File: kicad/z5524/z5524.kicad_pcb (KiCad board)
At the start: 4 copper layers, 80 x 80 mm, 21 parts, among them J1 Conn_01x01, J2 Conn_01x02, J3 Conn_02x20_Odd_Even, U13 LM4040AIM3-2.5, U14 AD5328, U15 M24C02-WMN, U7 PCA9555D

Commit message: schematic drafted- still needs some updates
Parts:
- removed G***: LOGO, project_footprints:zoxnoxious_small
- removed H1, H2, H3, H4: MountingHole, MountingHole:MountingHole_3.2mm_M3
- added C1: 0.1u, Capacitor_SMD:C_0603_1608Metric, F.Cu at (225.9, 34.9)
- added C10: 1u, Capacitor_SMD:C_1206_3216Metric, F.Cu at (170.7, 57.1)
- added C11: 1u, Capacitor_SMD:C_1206_3216Metric, F.Cu at (168.8, 62.8)
- added C12: 10n, Capacitor_SMD:C_0603_1608Metric, F.Cu at (214.0, 61.0)
- added C14: 1u, Capacitor_SMD:C_0603_1608Metric, F.Cu at (222.7, 53.4)
- added C15: 1u, Capacitor_SMD:C_0603_1608Metric, F.Cu at (218.0, 61.0)
- added C16: 1u, Capacitor_SMD:C_0603_1608Metric, F.Cu at (214.4, 58.5)
- added C17: 0.1u, Capacitor_SMD:C_0603_1608Metric, F.Cu at (218.4, 55.9)
- added C18: 0.1u, Capacitor_SMD:C_0603_1608Metric, F.Cu at (202.0, 63.0)
- added C19: 22n, Capacitor_SMD:C_0603_1608Metric, F.Cu at (221.9, 32.4)
- added C2: 0.1u, Capacitor_SMD:C_0603_1608Metric, F.Cu at (213.9, 30.3)
- added C20: 2u2, Capacitor_SMD:C_0603_1608Metric, F.Cu at (221.9, 34.9)
- added C21: 2u2, Capacitor_SMD:C_0603_1608Metric, F.Cu at (196.2, 89.1)
- added C22: 15n, Capacitor_SMD:C_0603_1608Metric, F.Cu at (217.5, 40.4)
- added C23: 1n, Capacitor_SMD:C_0603_1608Metric, F.Cu at (234.2, 24.9)
- added C26: 47n, Capacitor_SMD:C_0805_2012Metric, F.Cu at (205.7, 35.3)
- added C27: 22n, Capacitor_SMD:C_0603_1608Metric, F.Cu at (217.9, 30.3)
- added C28: 22n, Capacitor_SMD:C_0603_1608Metric, F.Cu at (209.9, 35.1)
- added C29: 22n, Capacitor_SMD:C_0603_1608Metric, F.Cu at (213.9, 27.8)
- added C3: 1u, Capacitor_SMD:C_1206_3216Metric_Pad1.33x1.80mm_HandSolder, F.Cu at (162.4, 68.6)
- added C30: 0.1u, Capacitor_SMD:C_0603_1608Metric, F.Cu at (254.7, 50.0)
- added C31: 0.1u, Capacitor_SMD:C_0603_1608Metric, F.Cu at (247.6, 52.5)
- added C32: 560pF, Capacitor_SMD:C_0603_1608Metric, F.Cu at (242.0, 60.0)
- added C33: 33nF, Capacitor_SMD:C_0603_1608Metric, F.Cu at (243.6, 53.3)
- added C34: 33nF, Capacitor_SMD:C_0603_1608Metric, F.Cu at (251.6, 52.5)
- added C35: 33nF, Capacitor_SMD:C_0603_1608Metric, F.Cu at (246.0, 58.4)
- added C36: 4.7u, Capacitor_THT:C_Rect_L7.2mm_W5.5mm_P5.00mm_FKS2_FKP2_MKS2_MKP2, F.Cu at (233.6, 49.7)
- added C38: 2n, Capacitor_SMD:C_1206_3216Metric, F.Cu at (234.5, 54.9)
- added C4: 1u, Capacitor_SMD:C_1206_3216Metric_Pad1.33x1.80mm_HandSolder, F.Cu at (177.4, 51.3)
- added C40: 0.1u, Capacitor_SMD:C_0603_1608Metric, F.Cu at (243.3, 32.4)
- added C41: 0.1u, Capacitor_SMD:C_0603_1608Metric, F.Cu at (251.3, 32.4)
- added C42: 0.1u, Capacitor_SMD:C_0603_1608Metric, F.Cu at (255.3, 29.9)
- added C43: 33p, Capacitor_SMD:C_0603_1608Metric, F.Cu at (243.3, 27.4)
- added C44: 33p, Capacitor_SMD:C_0603_1608Metric, F.Cu at (247.3, 29.9)
- added C45: 0.1u, Capacitor_SMD:C_0603_1608Metric, F.Cu at (204.6, 78.8)
- added C46: 0.1u, Capacitor_SMD:C_0603_1608Metric, F.Cu at (208.6, 76.8)
- added C47: 0.1u, Capacitor_SMD:C_0603_1608Metric, F.Cu at (204.6, 81.3)
- added C48: 10u, Capacitor_SMD:C_0805_2012Metric, F.Cu at (186.8, 25.1)
- added C49: 3.9n, Capacitor_SMD:C_0603_1608Metric, F.Cu at (185.1, 37.9)
- added C5: 0.1u, Capacitor_SMD:C_0603_1608Metric, F.Cu at (190.0, 58.5)
- added C50: 0.1u, Capacitor_SMD:C_0603_1608Metric, F.Cu at (204.9, 74.2)
- added C51: 100p, Capacitor_SMD:C_0805_2012Metric, F.Cu at (172.8, 37.8)
- added C52: 100p, Capacitor_SMD:C_0805_2012Metric, F.Cu at (166.5, 43.0)
- added C53: 100p, Capacitor_SMD:C_0805_2012Metric, F.Cu at (179.1, 31.6)
- added C54: 0.1u, Capacitor_SMD:C_0603_1608Metric, F.Cu at (208.6, 79.3)
- added C55: 0.1u, Capacitor_SMD:C_0603_1608Metric, F.Cu at (212.9, 74.2)
- added C56: 4u7, Capacitor_THT:CP_Radial_D4.0mm_P1.50mm, F.Cu at (181.1, 26.4)
- added C57: 4.7u, Capacitor_SMD:C_0805_2012Metric, F.Cu at (202.2, 57.8)
- added C58: 0.1u, Capacitor_SMD:C_0603_1608Metric, F.Cu at (210.7, 50.9)
- added C59: 100p, Capacitor_SMD:C_0603_1608Metric, F.Cu at (181.6, 62.3)
- added C6: 0.1u, Capacitor_SMD:C_0603_1608Metric, F.Cu at (186.0, 58.5)
- added C60: 0.1u, Capacitor_SMD:C_0603_1608Metric, F.Cu at (181.1, 68.3)
- added C61: 0.1u, Capacitor_SMD:C_0603_1608Metric, F.Cu at (185.6, 61.0)
- added C62: 100p, Capacitor_SMD:C_0603_1608Metric, F.Cu at (187.3, 50.9)
- added C63: 22n, Capacitor_SMD:C_0603_1608Metric, F.Cu at (206.4, 57.5)
- added C64: 0.1u, Capacitor_SMD:C_0603_1608Metric, F.Cu at (246.7, 47.4)
- added C65: 0.1u, Capacitor_SMD:C_0603_1608Metric, F.Cu at (254.7, 47.4)
- added C66: 5n, Capacitor_SMD:C_0603_1608Metric, F.Cu at (251.3, 24.9)
- added C67: 33p, Capacitor_SMD:C_0603_1608Metric, F.Cu at (255.3, 27.4)
- added C68: 0.1u, Capacitor_SMD:C_0603_1608Metric, F.Cu at (208.9, 74.2)
- added C69: 0.1u, Capacitor_SMD:C_0603_1608Metric, F.Cu at (212.6, 76.8)
- added C7: 0.1u, Capacitor_SMD:C_0603_1608Metric, F.Cu at (191.3, 50.9)
- added C70: 10n, Capacitor_SMD:C_0603_1608Metric, F.Cu at (177.0, 37.5)
- added C71: 10n, Capacitor_SMD:C_0603_1608Metric, F.Cu at (183.3, 32.9)
- added C72: 6.8n, Capacitor_SMD:C_0603_1608Metric, F.Cu at (222.4, 55.9)
- added C73: 6.8n, Capacitor_SMD:C_0603_1608Metric, F.Cu at (210.0, 62.5)
- added C74: 22n, Capacitor_SMD:C_0603_1608Metric, F.Cu at (221.5, 40.4)
- added C8: 0.1u, Capacitor_SMD:C_0603_1608Metric, F.Cu at (186.0, 55.9)
- added C9: 22n, Capacitor_SMD:C_0603_1608Metric, F.Cu at (206.0, 60.5)
- added D1: 1N5819WS, Diode_SMD:D_SOD-323, F.Cu at (214.0, 25.1)
- added D2: 1N4148WS, Diode_SMD:D_SOD-323, F.Cu at (239.5, 54.7)
- added D3: 1N4148WS, Diode_SMD:D_SOD-323, F.Cu at (233.8, 58.1)
- added D5: 1N4148WS, Diode_SMD:D_SOD-323, F.Cu at (242.6, 47.7)
- added D6: 1N4148WS, Diode_SMD:D_SOD-323, F.Cu at (242.6, 50.6)
- added Q1: 2N7002K, Package_TO_SOT_SMD:SOT-23, F.Cu at (161.9, 43.7)
- added R1: 1k, Resistor_SMD:R_1206_3216Metric, F.Cu at (176.3, 57.1)
- added R10: 5k1, Resistor_SMD:R_0603_1608Metric, F.Cu at (218.7, 53.4)
- added R11: 20k, Resistor_SMD:R_0603_1608Metric, F.Cu at (190.0, 55.9)
- added R12: 10k, Resistor_SMD:R_0603_1608Metric, F.Cu at (218.7, 50.9)
- added R13: 10k, Resistor_SMD:R_0603_1608Metric, F.Cu at (191.3, 53.4)
- added R14: 22k, Resistor_SMD:R_0603_1608Metric, F.Cu at (214.4, 55.9)
- added R15: 22k, Resistor_SMD:R_0603_1608Metric, F.Cu at (218.4, 58.5)
- added R16: 20k, Resistor_SMD:R_0603_1608Metric, F.Cu at (173.1, 68.3)
- added R17: 10k, Resistor_SMD:R_0603_1608Metric, F.Cu at (206.0, 63.0)
- added R18: 110, Resistor_SMD:R_0603_1608Metric, F.Cu at (218.0, 63.5)
- added R19: 110, Resistor_SMD:R_0603_1608Metric, F.Cu at (214.7, 50.9)
- added R2: 240, Resistor_SMD:R_1206_3216Metric, F.Cu at (168.2, 68.5)
- added R21: 110, Resistor_SMD:R_0603_1608Metric, F.Cu at (210.4, 57.5)
- added R22: 5k1, Resistor_SMD:R_0603_1608Metric, F.Cu at (217.9, 35.3)
- added R23: 110k, Resistor_SMD:R_0603_1608Metric, F.Cu at (213.9, 35.3)
- added R24: 10k, Resistor_SMD:R_0603_1608Metric, F.Cu at (221.9, 27.4)
- added R25: 20k, Resistor_SMD:R_0603_1608Metric, F.Cu at (229.9, 29.9)
- added R26: 47k, Resistor_SMD:R_0603_1608Metric, F.Cu at (225.5, 37.4)
- added R27: 20k, Resistor_SMD:R_0603_1608Metric, F.Cu at (225.9, 29.9)
- added R28: 36k, Resistor_SMD:R_0603_1608Metric, F.Cu at (209.5, 38.1)
- added R29: 30k, Resistor_SMD:R_0603_1608Metric, F.Cu at (213.5, 40.4)
- added R3: ?, Resistor_SMD:R_1206_3216Metric, F.Cu at (176.3, 60.4)
- added R30: 39k, Resistor_SMD:R_0603_1608Metric, F.Cu at (209.5, 40.6)
- added R31: 10k, Resistor_SMD:R_0603_1608Metric, F.Cu at (217.5, 37.8)
- added R32: 15k, Resistor_SMD:R_0603_1608Metric, F.Cu at (225.9, 32.4)
- added R33: 51k, Resistor_SMD:R_0603_1608Metric, F.Cu at (205.4, 38.1)
- added R34: 47k, Resistor_SMD:R_0603_1608Metric, F.Cu at (213.9, 32.8)
- added R35: 11k, Resistor_SMD:R_0603_1608Metric, F.Cu at (221.5, 37.8)
- added R36: 5k1, Resistor_SMD:R_0603_1608Metric, F.Cu at (217.9, 32.8)
- added R37: 22k, Resistor_SMD:R_0603_1608Metric, F.Cu at (225.9, 27.4)
- added R38: 4k7, Resistor_SMD:R_0603_1608Metric, F.Cu at (218.2, 24.9)
- added R39: 4k7, Resistor_SMD:R_0603_1608Metric, F.Cu at (226.2, 24.9)
- added R4: R, Resistor_SMD:R_0603_1608Metric, F.Cu at (177.6, 63.3)
- added R40: 5k1, Resistor_SMD:R_0603_1608Metric, F.Cu at (233.9, 27.4)
- added R41: 5k1, Resistor_SMD:R_0603_1608Metric, F.Cu at (229.9, 27.4)
- added R42: 100k, Resistor_SMD:R_0603_1608Metric, F.Cu at (205.4, 40.6)
- added R43: 5k1, Resistor_SMD:R_0603_1608Metric, F.Cu at (221.9, 29.9)
- added R44: 1M, Resistor_SMD:R_0603_1608Metric, F.Cu at (213.5, 37.8)
- added R45: 47k, Resistor_SMD:R_0603_1608Metric, F.Cu at (217.9, 27.8)
- added R46: 68k, Resistor_SMD:R_0603_1608Metric, F.Cu at (250.7, 50.0)
- added R48: 240k, Resistor_SMD:R_0603_1608Metric, F.Cu at (246.0, 55.9)
- added R49: 500, Resistor_SMD:R_0603_1608Metric, F.Cu at (250.7, 47.4)
- added R5: ?, Resistor_SMD:R_0603_1608Metric, F.Cu at (173.6, 63.3)
- added R50: 1k, Resistor_SMD:R_0603_1608Metric, F.Cu at (237.9, 57.8)
- added R51: 20k, Resistor_SMD:R_0603_1608Metric, F.Cu at (187.3, 53.4)
- added R52: 62k, Resistor_SMD:R_0603_1608Metric, F.Cu at (246.7, 50.0)
- added R53: 47k, Resistor_SMD:R_0603_1608Metric, F.Cu at (247.3, 24.9)
- added R54: 47k, Resistor_SMD:R_0603_1608Metric, F.Cu at (251.3, 29.9)
- added R55: 47k, Resistor_SMD:R_0603_1608Metric, F.Cu at (243.3, 24.9)
- added R57: 47k, Resistor_SMD:R_0603_1608Metric, F.Cu at (255.3, 24.9)
- added R58: 4k3, Resistor_SMD:R_0603_1608Metric, F.Cu at (178.8, 34.3)
- added R59: 47k, Resistor_SMD:R_0603_1608Metric, F.Cu at (191.1, 27.4)
- added R6: 13k, Resistor_SMD:R_0603_1608Metric, F.Cu at (177.1, 68.3)
- added R60: 49.9k, Resistor_SMD:R_0603_1608Metric, F.Cu at (180.6, 40.1)
- added R61: 10k, Resistor_SMD:R_0603_1608Metric, F.Cu at (189.1, 37.9)
- added R62: 270k, Resistor_SMD:R_0603_1608Metric, F.Cu at (185.1, 35.4)
- added R63: 100k, Resistor_SMD:R_0603_1608Metric, F.Cu at (183.3, 30.4)
- added R64: 22k, Resistor_SMD:R_0603_1608Metric, F.Cu at (186.6, 27.9)
- added R65: 270, Resistor_SMD:R_0603_1608Metric, F.Cu at (191.3, 32.4)
- added R66: 20k, Resistor_SMD:R_0603_1608Metric, F.Cu at (195.1, 27.4)
- added R67: 20k, Resistor_SMD:R_0603_1608Metric, F.Cu at (170.8, 43.1)
- added R68: 20k, Resistor_SMD:R_0603_1608Metric, F.Cu at (191.3, 29.9)
- added R69: 20k, Resistor_SMD:R_0603_1608Metric, F.Cu at (195.3, 32.4)
- added R7: 3k, Resistor_SMD:R_0603_1608Metric, F.Cu at (181.1, 65.8)
- added R70: 20k, Resistor_SMD:R_0603_1608Metric, F.Cu at (178.8, 43.1)
- added R71: 20k, Resistor_SMD:R_0603_1608Metric, F.Cu at (187.3, 32.9)
- added R72: 100, Resistor_SMD:R_0603_1608Metric, F.Cu at (176.6, 40.6)
- added R73: 100k, Resistor_SMD:R_0603_1608Metric, F.Cu at (182.8, 42.6)
- added R74: 20k, Resistor_SMD:R_0603_1608Metric, F.Cu at (195.3, 29.9)
- added R75: 499k, Resistor_SMD:R_0603_1608Metric, F.Cu at (191.1, 24.9)
- added R76: 10k, Resistor_SMD:R_0603_1608Metric, F.Cu at (172.6, 40.6)
- added R77: 5k1, Resistor_SMD:R_0603_1608Metric, F.Cu at (214.7, 53.4)
- added R78: 22k, Resistor_SMD:R_0603_1608Metric, F.Cu at (210.0, 60.0)
- added R79: 1k, Resistor_SMD:R_0603_1608Metric, F.Cu at (242.0, 57.4)
- added R8: 6k8, Resistor_SMD:R_0603_1608Metric, F.Cu at (185.6, 63.5)
- added R80: 62k, Resistor_SMD:R_0603_1608Metric, F.Cu at (250.0, 55.0)
- added R81: 100, Resistor_SMD:R_0603_1608Metric, F.Cu at (247.3, 27.4)
- added R82: 4k7, Resistor_SMD:R_0603_1608Metric, F.Cu at (174.8, 43.1)
- added R83: 4k7, Resistor_SMD:R_0603_1608Metric, F.Cu at (189.1, 35.4)
- added R84: 4k7, Resistor_SMD:R_0603_1608Metric, F.Cu at (195.1, 24.9)
- added R85: 47k, Resistor_SMD:R_0603_1608Metric, F.Cu at (251.3, 27.4)
- added R86: 47k, Resistor_SMD:R_0603_1608Metric, F.Cu at (247.3, 32.4)
- added R87: 47k, Resistor_SMD:R_0603_1608Metric, F.Cu at (243.3, 29.9)
- added R88: 10k, Resistor_SMD:R_0603_1608Metric, F.Cu at (187.3, 30.4)
- added R89: 10k, Resistor_SMD:R_0603_1608Metric, F.Cu at (181.0, 36.8)
- added R9: 6k8, Resistor_SMD:R_0603_1608Metric, F.Cu at (173.1, 65.8)
- added R90: 1k, Resistor_SMD:R_0603_1608Metric, F.Cu at (181.1, 59.8)
- added R91: 1k, Resistor_SMD:R_0603_1608Metric, F.Cu at (177.1, 65.8)
- added R92: 18k, Resistor_SMD:R_0603_1608Metric, F.Cu at (222.7, 50.9)
- added R93: 18k, Resistor_SMD:R_0603_1608Metric, F.Cu at (214.0, 63.5)
- added R94: 82k, Resistor_SMD:R_0603_1608Metric, F.Cu at (210.7, 53.4)
- added R95: 82k, Resistor_SMD:R_0603_1608Metric, F.Cu at (202.0, 60.5)
- added R96: 10k, Resistor_SMD:R_0603_1608Metric, F.Cu at (230.2, 24.9)
- added R97: 10k, Resistor_SMD:R_0603_1608Metric, F.Cu at (222.2, 24.9)
- added RV1: 5k, Potentiometer_THT:Potentiometer_Bourns_3296W_Vertical, F.Cu at (176.0, 26.8)
- added RV2: 5k, Potentiometer_THT:Potentiometer_Bourns_3296W_Vertical, F.Cu at (172.8, 98.4)
- added RV3: 5k, Potentiometer_THT:Potentiometer_Bourns_3296W_Vertical, F.Cu at (167.6, 38.3)
- added U1: TL074, Package_SO:TSSOP-14_4.4x5mm_P0.65mm, F.Cu at (207.7, 28.7)
- added U10: TL072, Package_SO:SO-8_3.9x4.9mm_P1.27mm, F.Cu at (181.9, 76.2)
- added U11: NE5532, Package_SO:SOIC-8_3.9x4.9mm_P1.27mm, F.Cu at (180.1, 98.4)
- added U12: TL074, Package_SO:TSSOP-14_4.4x5mm_P0.65mm, F.Cu at (222.7, 85.8)
- added U16: SSI2130, Package_DFN_QFN:QFN-32-1EP_4x4mm_P0.4mm_EP2.65x2.65mm, F.Cu at (173.7, 33.2)
- added U17: DG442xY, Package_SO:SOIC-16_3.9x9.9mm_P1.27mm, F.Cu at (163.7, 29.3)
- added U18: TL072, Package_SO:SO-8_3.9x4.9mm_P1.27mm, F.Cu at (198.4, 80.8)
- added U19: LM311, Package_SO:TSSOP-8_4.4x3mm_P0.65mm, F.Cu at (198.5, 75.3)
- added U2: LM337L_TO92, Package_TO_SOT_THT:TO-92_Inline, F.Cu at (161.4, 64.4)
- added U21: AD5328, Package_SO:TSSOP-16_4.4x5mm_P0.65mm, F.Cu at (204.3, 53.0)
- added U3: LM4040BIM3-2.5, Package_TO_SOT_SMD:SOT-23, F.Cu at (181.6, 56.3)
- added U4: LM4040BIM3-4.1, Package_TO_SOT_SMD:SOT-23, F.Cu at (182.8, 51.9)
- added U5: DG442xY, Package_SO:SOIC-16_3.9x9.9mm_P1.27mm, F.Cu at (163.7, 55.4)
- added U6: TL072, Package_SO:SO-8_3.9x4.9mm_P1.27mm, F.Cu at (222.5, 76.2)
- added U8: LM78L05_TO92, Package_TO_SOT_THT:TO-92_Inline, F.Cu at (169.9, 52.9)
- added U9: AS3394, Package_SO:SOIC-24W_7.5x15.4mm_P1.27mm, F.Cu at (171.2, 81.5)
- R47: value 4k7 -> 1k; footprint Resistor_SMD:R_1206_3216Metric -> Resistor_SMD:R_0603_1608Metric
- U13: value LM4040AIM3-2.5 -> AS3364; footprint Package_TO_SOT_SMD:SOT-23 -> Package_SO:SOIC-16_3.9x9.9mm_P1.27mm
- moved J1 13.9 mm to (55.7, 72.1)
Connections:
- C39 pad 1: /DAC/VREF_2.5V -> +12V
- J3 pad 21: /CARD1_OUT1 -> unconnected-(J3-Pad21)
- J3 pad 22: /CARD1_OUT2 -> unconnected-(J3-Pad22)
- J3 pad 23: /CARD2_OUT1 -> unconnected-(J3-Pad23)
- J3 pad 25: /CARD2_OUT2 -> unconnected-(J3-Pad25)
- J3 pad 26: /CARD3_OUT1 -> unconnected-(J3-Pad26)
- J3 pad 27: /CARD3_OUT2 -> unconnected-(J3-Pad27)
- J3 pad 29: /CARD4_OUT1 -> unconnected-(J3-Pad29)
- J3 pad 3: /SPI_MISO -> unconnected-(J3-Pad3)
- J3 pad 30: /CARD4_OUT2 -> unconnected-(J3-Pad30)
- J3 pad 31: /CARD5_OUT1 -> unconnected-(J3-Pad31)
- J3 pad 33: /CARD5_OUT2 -> unconnected-(J3-Pad33)
- J3 pad 34: /CARD6_OUT1 -> unconnected-(J3-Pad34)
- J3 pad 35: /CARD6_OUT2 -> unconnected-(J3-Pad35)
- J3 pad 37: /CARD7_OUT1 -> unconnected-(J3-Pad37)
- R47 pad 1: +5V -> GND
- R47 pad 2: /DAC/VREF_2.5V -> /AS3394/3394_EXT_IN
- U13 pad 1: /DAC/VREF_2.5V -> Net-(R81-Pad2)
- U13 pad 2: GND -> Net-(R53-Pad2)
- U13 pad 3: (no net) -> /SSI2130_MOD_CV
- U14 pad 10: unconnected-(U14-Pad10) -> /DAC 3394/RES_DAC_CV
- U14 pad 11: unconnected-(U14-Pad11) -> /DAC 3394/MOD_AMT_DAC_CV
- U14 pad 12: unconnected-(U14-Pad12) -> /DAC 3394/FINAL_GAIN_DAC_CV
- U14 pad 13: unconnected-(U14-Pad13) -> /DAC 3394/SSI2130_MOD_DAC_CV
- U14 pad 2: /SPI_CS0 -> /SPI_CS1
- U14 pad 4: unconnected-(U14-Pad4) -> /DAC 3394/VCO_DAC_CV
- U14 pad 5: unconnected-(U14-Pad5) -> /DAC 3394/PWM_DAC_CV
- U14 pad 6: unconnected-(U14-Pad6) -> /DAC 3394/Mix_DAC_CV
- U14 pad 7: unconnected-(U14-Pad7) -> /DAC 3394/VCF_DAC_CV
- U14 pad 8: /DAC/VREF_2.5V -> /VREF_4.096
- U14 pad 9: /DAC/VREF_2.5V -> /VREF_4.096
- U7 pad 11: unconnected-(U7-Pad11) -> /LED_CTRL
- U7 pad 17: unconnected-(U7-Pad17) -> /SOFTSYNC_2130_CTRL
- U7 pad 18: unconnected-(U7-Pad18) -> /HARDSYNC_2130_CTRL
- U7 pad 19: unconnected-(U7-Pad19) -> /FM2130_MOD_CTRL
- U7 pad 20: unconnected-(U7-Pad20) -> /PWM2130_MOD_CTRL
- U7 pad 4: unconnected-(U7-Pad4) -> /VCO3394_EXP_MOD_CTRL
- U7 pad 5: unconnected-(U7-Pad5) -> /VCF3394_MOD_CTRL
- U7 pad 6: unconnected-(U7-Pad6) -> /PWM3394_MOD_CTRL
- U7 pad 7: /LED_CTRL -> /WAVESELECT_MOD_CTRL
- U7 pad 8: unconnected-(U7-Pad8) -> /WAVESELECT_1
- U7 pad 9: unconnected-(U7-Pad9) -> /WAVESELECT_2
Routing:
- net /SPI_CS0: track 64.4 -> 0.00 mm
- net /SPI_CLK: track 54.4 -> 0.00 mm
- net /SPI_MOSI: track 54.4 -> 0.00 mm, vias 1 -> 0
- net /I2C_ADDR0: track 33.6 -> 0.00 mm, vias 2 -> 0
- net /SDA1: track 27.8 -> 0.00 mm, vias 2 -> 0
- net /I2C_ADDR1: track 27.5 -> 0.00 mm
- net /SCL1: track 27.4 -> 0.00 mm, vias 1 -> 0
- net /I2C_ADDR2: track 24.3 -> 0.00 mm
- net +5V: track 21.5 -> 0.00 mm, vias 6 -> 0
- net /DAC/VREF_2.5V: track 17.6 -> 0.00 mm
- net GND: track 114.9 -> 97.5 mm, vias 10 -> 0
- net /LED_CTRL: track 10.9 -> 0.00 mm
- net Net-(J2-Pad1): track 10.5 -> 0.00 mm
- net Net-(D4-Pad1): track 1.89 -> 0.00 mm
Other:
- board text removed: "BEYOND OBNOXIOUS"

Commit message: toying more with some placement
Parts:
- C32: value 560pF -> 560p
- C33, C34, C35: value 33nF -> 33n
- C36: value 4.7u -> 4u7; footprint Capacitor_THT:C_Rect_L7.2mm_W5.5mm_P5.00mm_FKS2_FKP2_MKS2_MKP2 -> Capacitor_THT:CP_Radial_D4.0mm_P1.50mm
- C51, C52, C53: footprint Capacitor_SMD:C_0805_2012Metric -> Capacitor_SMD:C_0603_1608Metric
- moved C42 190.5 mm to (69.9, 73.7), turned to -90 degrees
- moved R54 182.5 mm to (71.7, 62.2), turned to -90 degrees
- moved R87 180.8 mm to (67.9, 73.7), turned to -90 degrees
- moved R85 176.4 mm to (78.4, 62.2), turned to -90 degrees
- moved R53 176.1 mm to (78.1, 73.8), turned to 90 degrees
- moved C41 175.2 mm to (80.9, 73.0)
- moved C67 173.8 mm to (85.2, 63.0), turned to 180 degrees
- moved C66 173.0 mm to (82.4, 62.2), turned to -90 degrees
- moved R81 170.5 mm to (80.4, 62.2), turned to -90 degrees
- moved R57 168.9 mm to (90.8, 63.0)
- moved R55 165.6 mm to (85.0, 73.4)
- moved C43 165.4 mm to (85.0, 75.4), turned to 180 degrees
- moved R86 164.6 mm to (85.2, 61.0)
- moved R96 161.8 mm to (76.0, 73.8), turned to 90 degrees
- moved C40 161.0 mm to (87.8, 74.2), turned to -90 degrees
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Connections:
- U12 pad 1: /SSI2130_MOD -> /AS3394_MOD
- U12 pad 2: Net-(C43-Pad1) -> Net-(C44-Pad1)
- U12 pad 6: Net-(C44-Pad1) -> Net-(C67-Pad1)
- U12 pad 7: /AS3394_MOD -> /AS3394_SINE_MOD
- U12 pad 8: /AS3394_SINE_MOD -> /SSI2130_MOD
- U12 pad 9: Net-(C67-Pad1) -> Net-(C43-Pad1)
- U13 pad 10: Net-(R85-Pad2) -> Net-(R87-Pad1)
- U13 pad 11: /AS3394_SINE_CV -> GND
- U13 pad 12: Net-(C67-Pad1) -> unconnected-(U13-Pad12)
- U13 pad 13: unconnected-(U13-Pad13) -> Net-(C43-Pad1)
- U13 pad 14: GND -> /SSI2130_MOD_CV
- U13 pad 15: Net-(R87-Pad1) -> Net-(R53-Pad2)
- U13 pad 16: (no net) -> +12V
- U13 pad 2: Net-(R53-Pad2) -> Net-(R85-Pad2)
- U13 pad 3: /SSI2130_MOD_CV -> /AS3394_SINE_CV
- U13 pad 4: Net-(C43-Pad1) -> Net-(C67-Pad1)

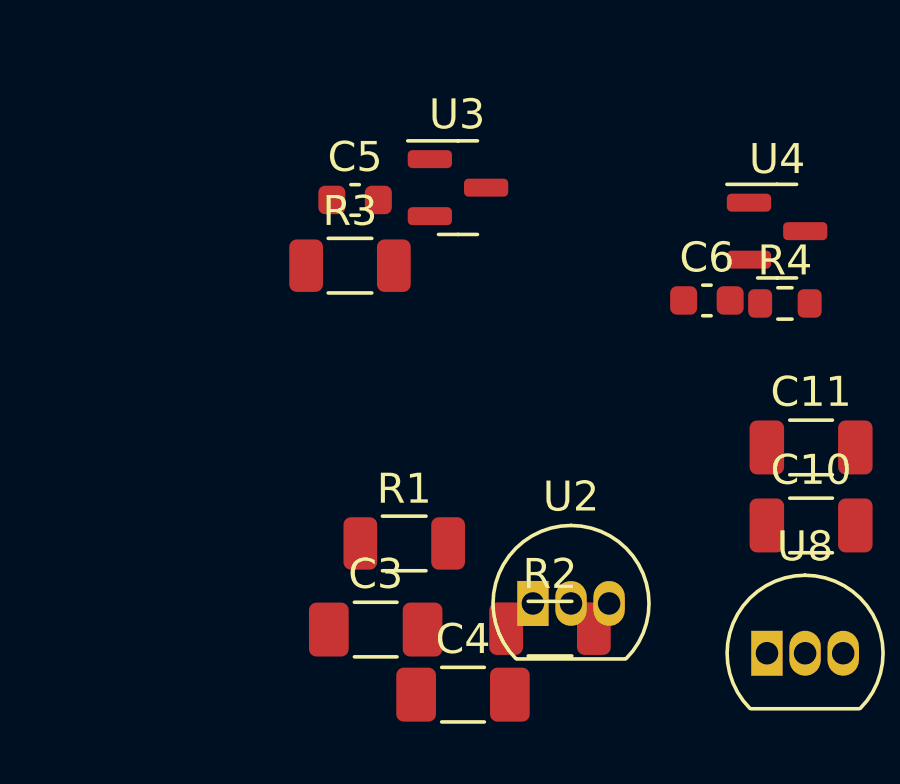
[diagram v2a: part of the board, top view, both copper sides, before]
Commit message: calc Vref resistors and fix a couple errors
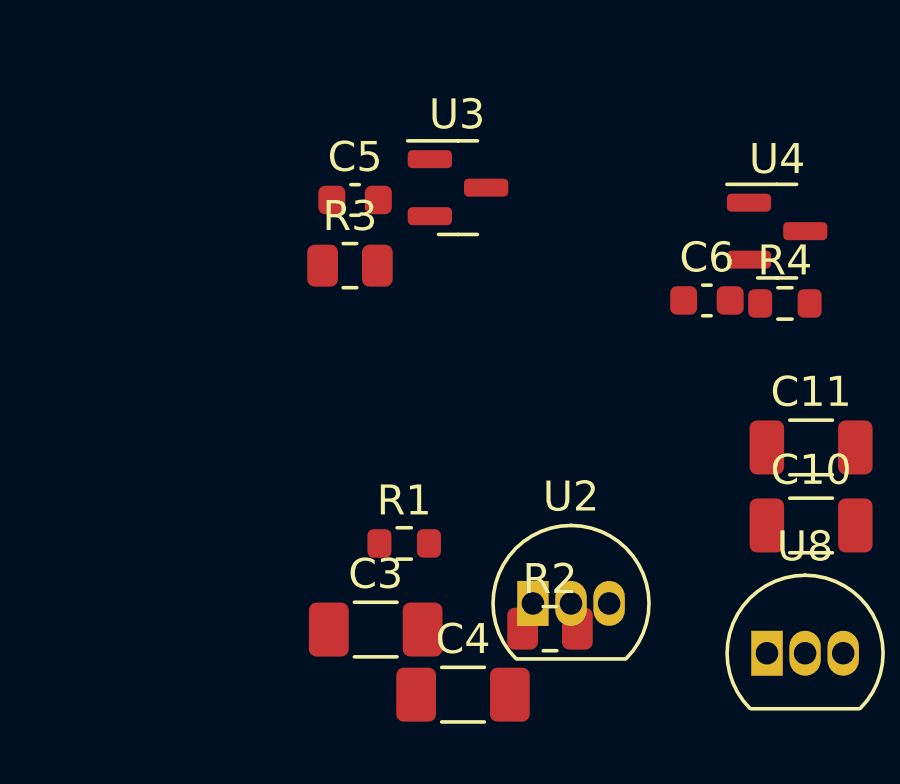
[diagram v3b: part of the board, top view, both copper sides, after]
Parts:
- R1: footprint Resistor_SMD:R_1206_3216Metric -> Resistor_SMD:R_0603_1608Metric
- R2: footprint Resistor_SMD:R_1206_3216Metric -> Resistor_SMD:R_0805_2012Metric
- R3: value ? -> 2k4; footprint Resistor_SMD:R_1206_3216Metric -> Resistor_SMD:R_0805_2012Metric
- R4: value R -> 1k
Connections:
- net /DAC 3394/Mix_DAC_CV renamed /DAC 3394/MIX_DAC_CV
- R46 pad 1: /VCO_SSI2130 -> /SSI2130_VCO
- R5 pad 1: /VCO_SSI2130 -> /SSI2130_MOD
- RV3 pad 1: GND -> /SSI2130/VREF
- RV3 pad 2: /SSI2130/VREF -> Net-(R88-Pad1)
- RV3 pad 3: Net-(R88-Pad1) -> GND

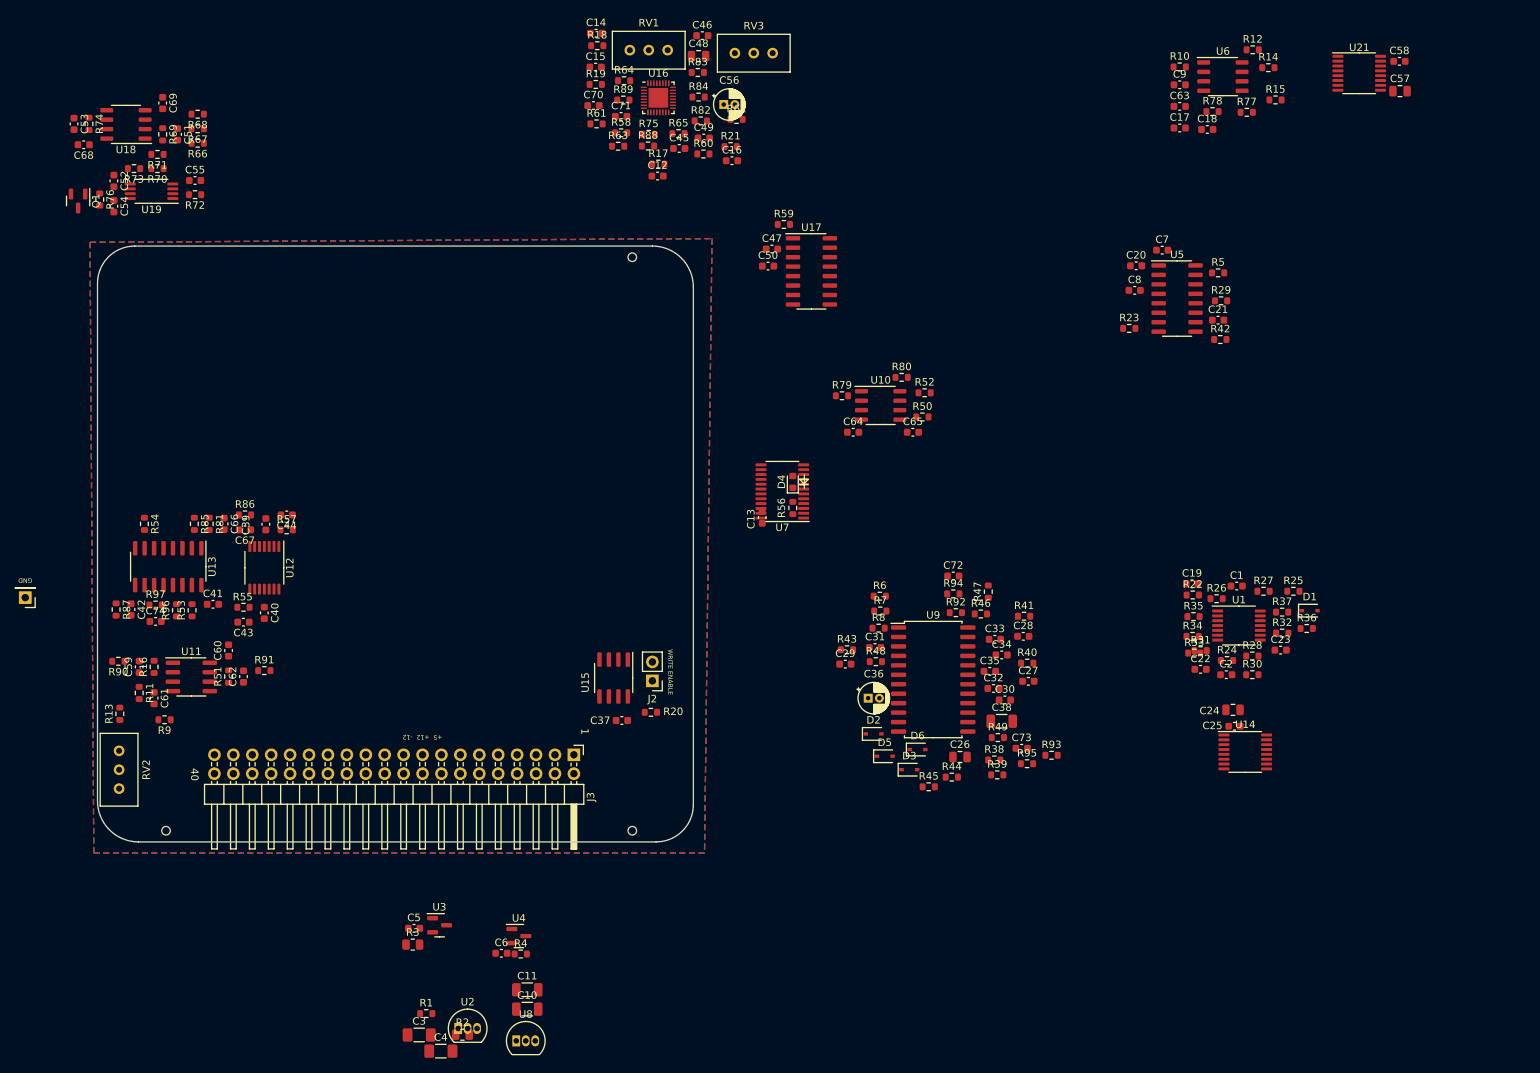
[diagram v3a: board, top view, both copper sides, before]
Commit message: modify footprint; modify some schematic values
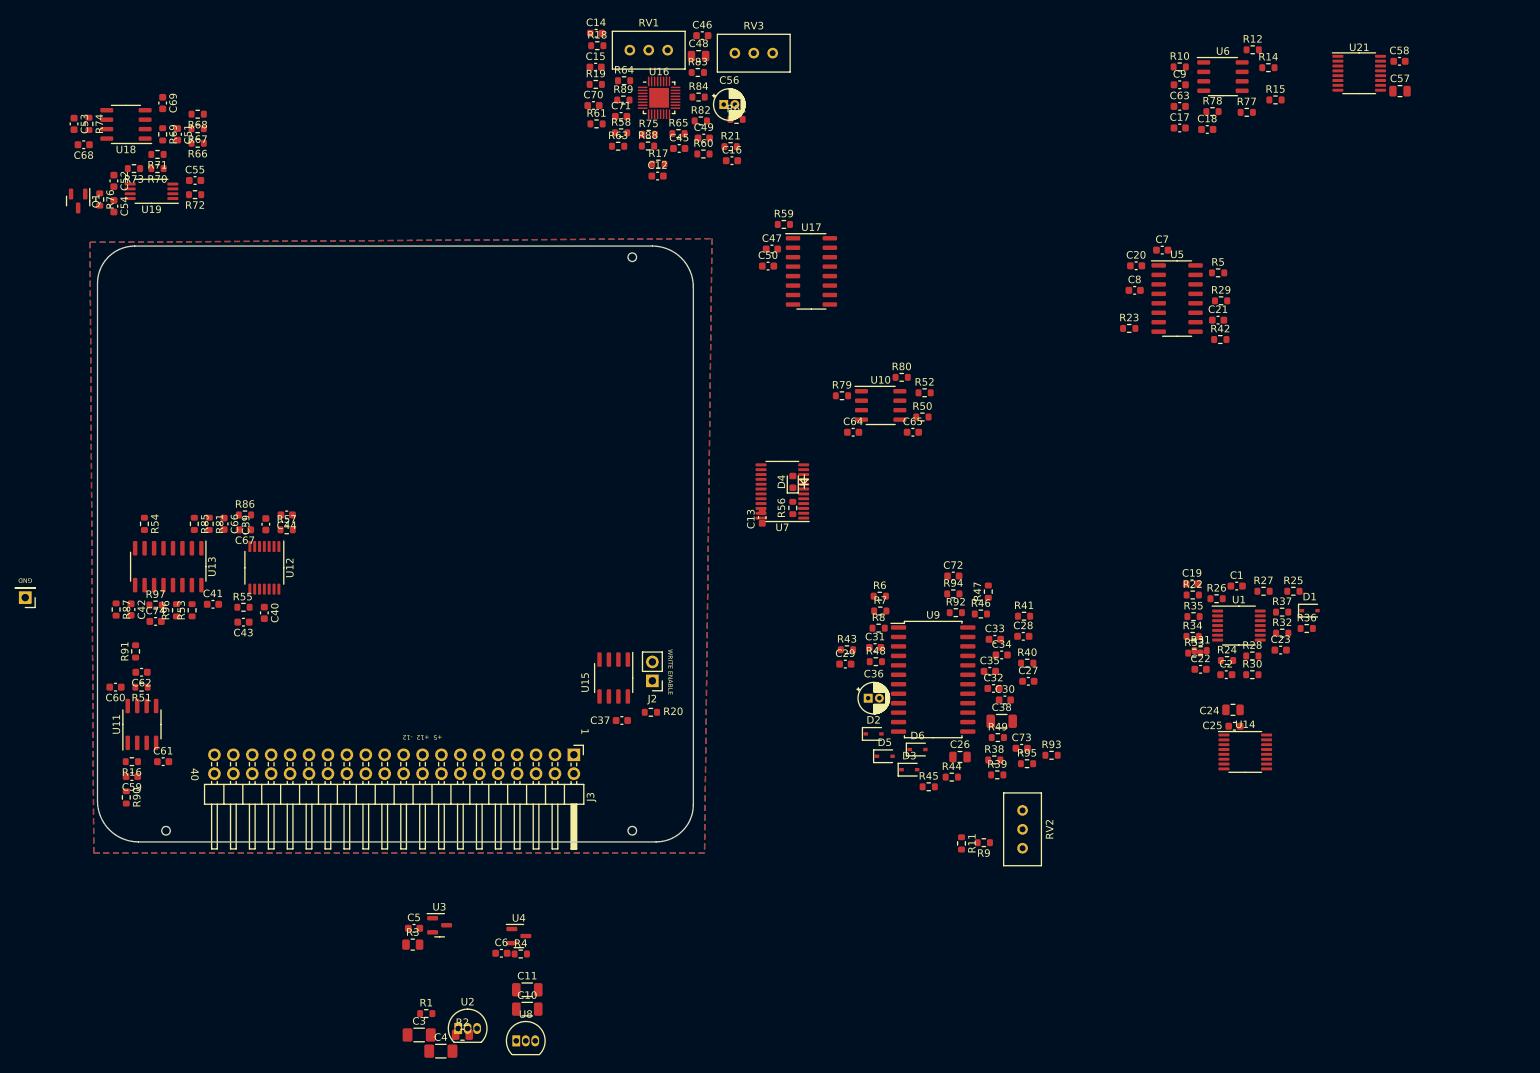
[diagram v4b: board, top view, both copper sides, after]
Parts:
- removed R13: 10k, Resistor_SMD:R_0603_1608Metric
- R11: value 20k -> 13k
- R5: value ? -> 10k
- R6: value 13k -> 20k
- R7: value 3k -> 39k
- R8: value 6k8 -> 10k
- R9: value 6k8 -> 8k2
- RV2: value 5k -> 200
- U16: footprint Package_DFN_QFN:QFN-32-1EP_4x4mm_P0.4mm_EP2.65x2.65mm -> Package_DFN_QFN:QFN-32-1EP_4x4mm_P0.4mm_EP2.65x2.65mm_Handsolder
- moved RV2 121.6 mm to (189.6, 105.8)
- moved R11 112.2 mm to (181.4, 105.1)
- moved R9 111.2 mm to (184.4, 105.0)
- moved R90 18.3 mm to (69.3, 98.9), turned to -90 degrees
- moved R91 17.5 mm to (70.5, 79.3), turned to 90 degrees
- moved C60 16.0 mm to (67.8, 84.1), turned to 180 degrees
- moved C59 14.8 mm to (70.0, 96.1), turned to 180 degrees
- moved C62 13.7 mm to (71.3, 82.1), turned to 180 degrees
- moved R16 13.1 mm to (70.0, 94.1), turned to 180 degrees
- moved R51 11.8 mm to (71.3, 84.1), turned to 180 degrees
- moved U11 9.20 mm to (71.4, 89.1), turned to 90 degrees
- moved C61 8.61 mm to (74.2, 94.1), turned to 0 degrees
- moved U16 0.10 mm to (140.8, 5.00)
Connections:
- R11 pad 1: /SSI2130/MIX_OUT -> Net-(R11-Pad1)
- R11 pad 2: Net-(R11-Pad2) -> -6V
- RV2 pad 1: Net-(R9-Pad2) -> Net-(R11-Pad1)
- RV2 pad 2: Net-(R11-Pad2) -> /AS3394/3394_EXT_IN
- RV2 pad 3: Net-(R13-Pad1) -> Net-(R9-Pad2)
